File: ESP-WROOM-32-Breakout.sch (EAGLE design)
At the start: 11 parts, among them Q1 2N7002, SW1 PROG, SW2 RST, U3 ESP-WROOM-32

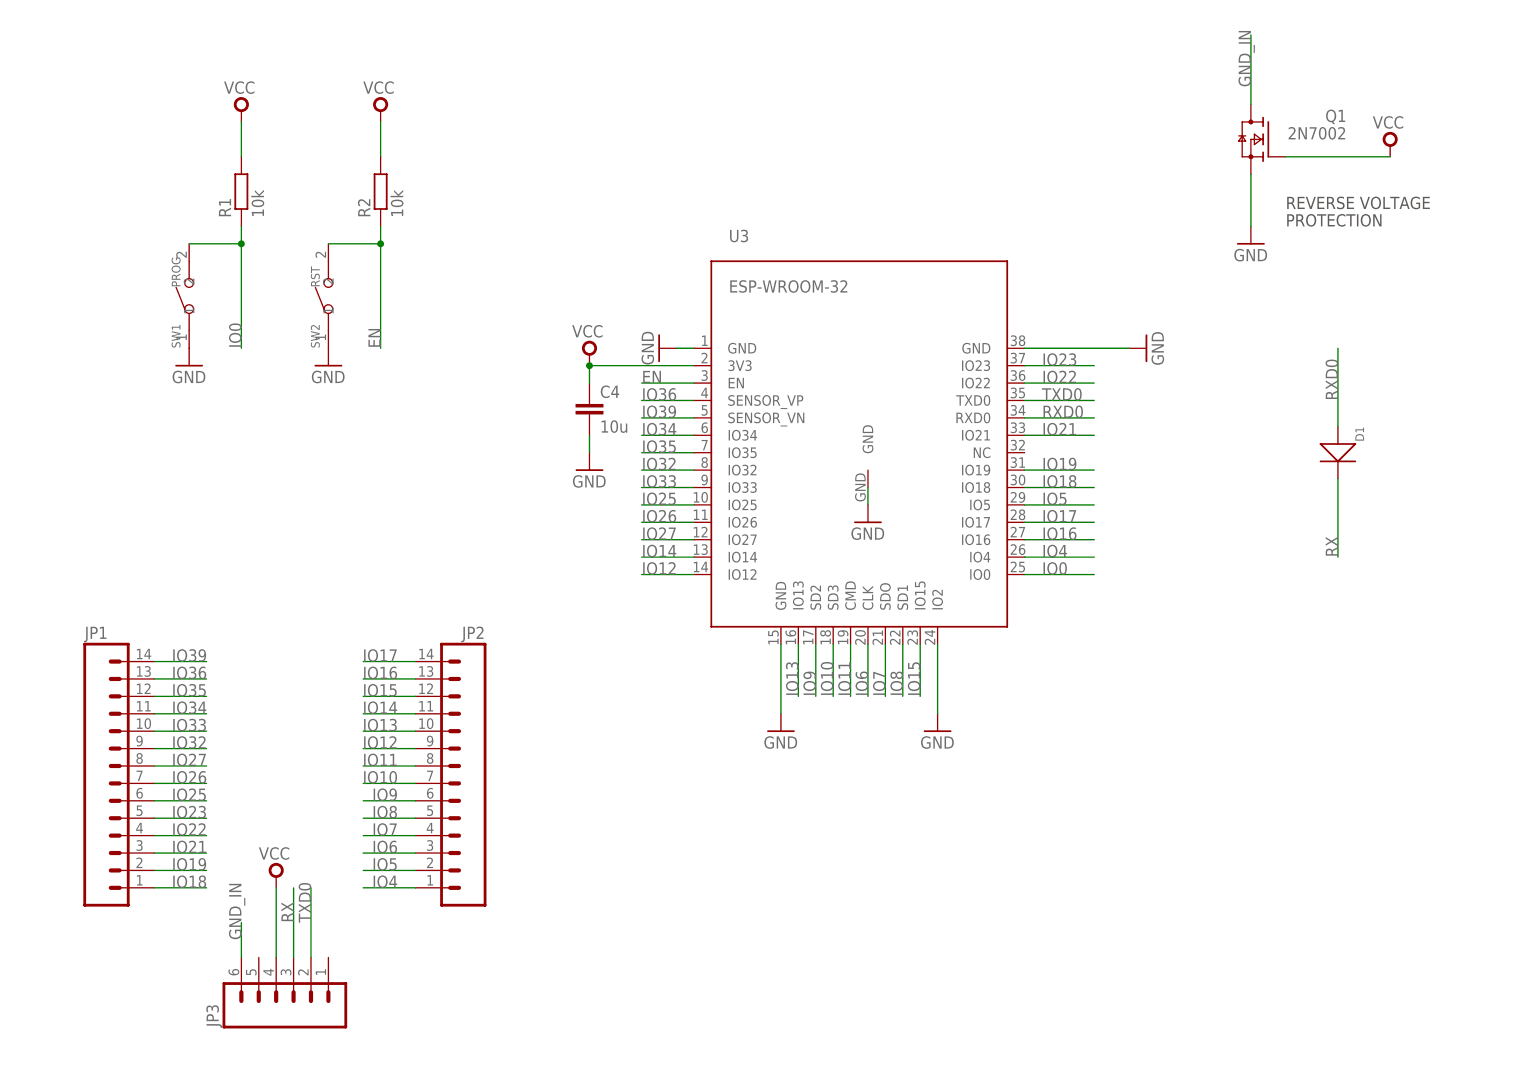
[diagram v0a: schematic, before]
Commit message: Updated layout, added 3,3V regulators
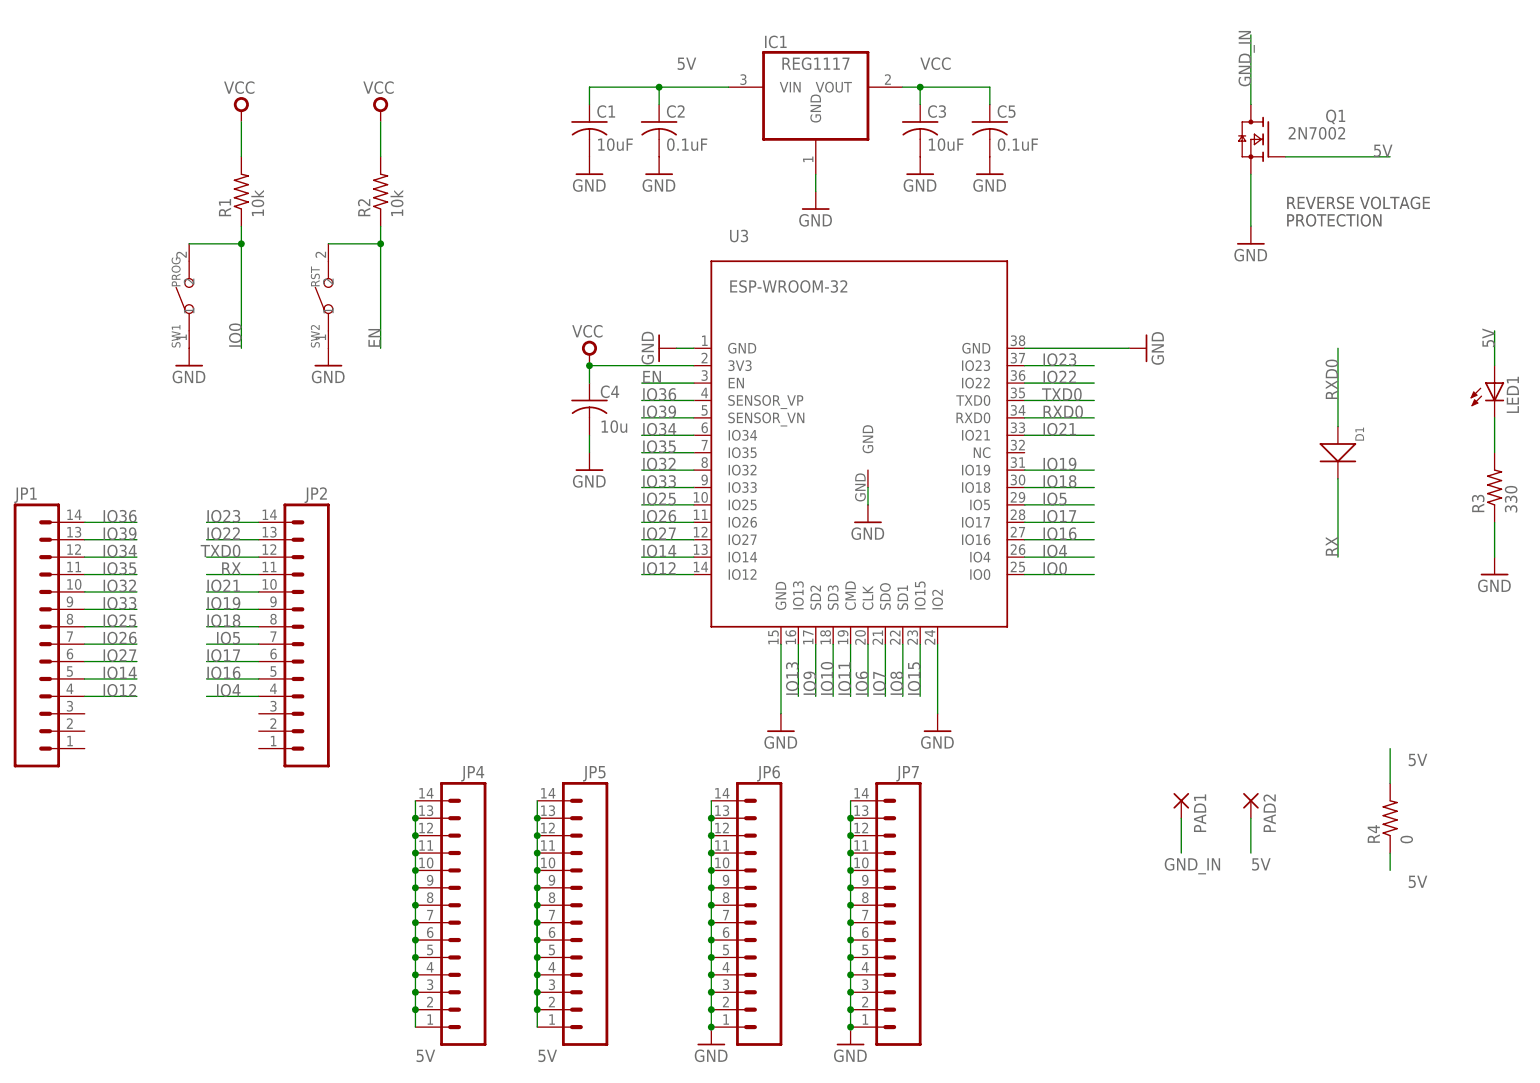
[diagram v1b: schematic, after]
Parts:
- removed JP3: (no value), SparkFun-Connectors:M06SILK_FEMALE_PTH
- added C1, C3: 10uF, adafruit:C-USC1206
- added C2, C5: 0.1uF, adafruit:C-USC1206
- added IC1: REG1117, burr-brown:REG1117
- added JP4, JP5, JP6, JP7: (no value), SparkFun-Connectors:M14
- added LED1: (no value), adafruit:LEDCHIPLED_1206
- added PAD1, PAD2: (no value), wirepad:SMD5
- added R3: 330, adafruit:R-US_R1206
- added R4: 0, adafruit:R-US_R1206
- C4: device rcl:C-EUC0603 -> adafruit:C-USC1206
- R1, R2: device rcl:R-EU_R0603 -> adafruit:R-US_R1206
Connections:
- new net 5V: C1.1, C2.1, IC1.VIN, JP4.1, JP4.10, JP4.11, JP4.12, JP4.13, JP4.14, JP4.2, JP4.3, JP4.4, JP4.5, JP4.6, JP4.7, JP4.8, JP4.9, JP5.1, JP5.10, JP5.11, JP5.12, JP5.13, JP5.14, JP5.2, JP5.3, JP5.4, JP5.5, JP5.6, JP5.7, JP5.8, JP5.9, LED1.A, PAD2.P, Q1.G, R4.1, R4.2
- new net N$1: LED1.C, R3.2
- net GND: now also C1.2, C2.2, C3.2, C5.2, IC1.GND, JP6.1, JP6.10, JP6.11, JP6.12, JP6.13, JP6.14, JP6.2, JP6.3, JP6.4, JP6.5, JP6.6, JP6.7, JP6.8, JP6.9, JP7.1, JP7.10, JP7.11, JP7.12, JP7.13, JP7.14, JP7.2, JP7.3, JP7.4, JP7.5, JP7.6, JP7.7, JP7.8, JP7.9, R3.1
- net GND_IN: now also PAD1.P; no longer JP3.6
- net IO10: no longer JP2.7
- net IO11: no longer JP2.8
- net IO12: now also JP1.4; no longer JP2.9
- net IO13: no longer JP2.10
- net IO14: now also JP1.5; no longer JP2.11
- net IO15: no longer JP2.12
- net IO16: now also JP2.5; no longer JP2.13
- net IO17: now also JP2.6; no longer JP2.14
- net IO18: now also JP2.8; no longer JP1.1
- net IO19: now also JP2.9; no longer JP1.2
- net IO21: now also JP2.10; no longer JP1.3
- net IO22: now also JP2.13; no longer JP1.4
- net IO23: now also JP2.14; no longer JP1.5
- net IO25: now also JP1.8; no longer JP1.6
- net IO27: now also JP1.6; no longer JP1.8
- net IO32: now also JP1.10; no longer JP1.9
- net IO33: now also JP1.9; no longer JP1.10
- net IO34: now also JP1.12; no longer JP1.11
- net IO35: now also JP1.11; no longer JP1.12
- net IO36: now also JP1.14; no longer JP1.13
- net IO39: now also JP1.13; no longer JP1.14
- net IO4: now also JP2.4; no longer JP2.1
- net IO5: now also JP2.7; no longer JP2.2
- net IO6: no longer JP2.3
- net IO7: no longer JP2.4
- net IO8: no longer JP2.5
- net IO9: no longer JP2.6
- net RX: now also JP2.11; no longer JP3.3
- net TXD0: now also JP2.12; no longer JP3.2
- net VCC: now also C3.1, C5.1, IC1.VOUT; no longer JP3.4, Q1.G
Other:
- moved on the sheet: JP1, JP2
